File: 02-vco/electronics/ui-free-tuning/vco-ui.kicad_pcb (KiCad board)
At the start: 2 copper layers, 58 x 110 mm, 40 parts, among them J1 Conn_01x04, J2 Conn_02x05_Odd_Even, J3 Conn_02x03_Odd_Even, J4 Conn_01x02, J5 Conn_02x02_Counter_Clockwise, J6 Conn_01x06, U1 0203

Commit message: Added VCO output to default connector
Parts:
- J6: value Conn_01x06 -> Conn_01x07; footprint Connector_PinSocket_2.54mm:PinSocket_1x06_P2.54mm_Vertical -> Connector_PinSocket_2.54mm:PinSocket_1x07_P2.54mm_Vertical
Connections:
- J6 pad 6: OUT_DEFAULT -> OUT_OUT
- J_OUT1 pad T: Net-(J_OUT1-PadT) -> OUT_OUT
- U1 pad 1: Net-(J_OUT1-PadT) -> OUT_OUT
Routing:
- net OUT_OUT: track 0.00 -> 163.4 mm
- net Net-(J_OUT1-PadT): track 131.6 -> 0.00 mm
- net OUT_DEFAULT: track 39.9 -> 36.5 mm
- net SUB: track 36.9 -> 38.0 mm, vias 0 -> 2
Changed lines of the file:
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@@
 	(net 19 "EXTRA_DEFAULT")
 	(net 20 "OUT_DEFAULT")
-	(net 21 "Net-(J_OUT1-PadT)")
+	(net 21 "OUT_OUT")
 	(net 22 "Net-(J_PWM1-PadT)")
 	(net 23 "Net-(R1-Pad2)")
@@
 			(layers "*.Cu" "*.Mask")
 			(remove_unused_layers no)
-			(net 21 "Net-(J_OUT1-PadT)")
+			(net 21 "OUT_OUT")
 			(pinfunction "1")
 			(pintype "output")
@@
 			(layers "*.Cu" "*.Mask")
 			(remove_unused_layers no)
-			(net 21 "Net-(J_OUT1-PadT)")
+			(net 21 "OUT_OUT")
 			(pintype "bidirectional")
 		)
@@
 		)
 	)
-	(footprint "Connector_PinSocket_2.54mm:PinSocket_1x06_P2.54mm_Vertical"
+	(footprint "Connector_PinSocket_2.54mm:PinSocket_1x07_P2.54mm_Vertical"
 		(locked yes)
 		(layer "B.Cu")
 		(at 132.5 151 -90)
-		(descr "Through hole straight socket strip, 1x06, 2.54mm pitch, single row (from Kicad 4.0.7), script generated")
-		(tags "Through hole socket strip THT 1x06 2.54mm single row")
+		(descr "Through hole straight socket strip, 1x07, 2.54mm pitch, single row (from Kicad 4.0.7), script generated")
+		(tags "Through hole socket strip THT 1x07 2.54mm single row")
 		(property "Reference" "J6"
-			(at -1.966 -15.122 0)
-			(layer "B.SilkS")
+			(at 0 2.77 90)
+			(layer "User.1")
 			(effects
 				(font
@@
 			)
 		)
-		(property "Value" "Conn_01x06"
-			(at 0 -15.47 90)
+		(property "Value" "Conn_01x07"
+			(at 0 -18.01 90)
 			(layer "B.Fab")
 			(effects
@@
 			)
 		)
-		(property "Description" "Generic connector, single row, 01x06, script generated (kicad-library-utils/schlib/autogen/connector/)"
+		(property "Description" "Generic connector, single row, 01x07, script generated (kicad-library-utils/schlib/autogen/connector/)"
 			(at 0 0 90)
 			(layer "B.Fab")
@@
 		)
 		(property "Part URL" "https://mou.sr/4lnf48h"
-			(at 0 0 90)
+			(at 0 0 270)
 			(unlocked yes)
 			(layer "B.Fab")
@@
 		)
 		(property "Vendor" "Mouser"
-			(at 0 0 90)
+			(at 0 0 270)
 			(unlocked yes)
 			(layer "B.Fab")
@@
 		)
 		(property "LCSC" ""
-			(at 0 0 90)
+			(at 0 0 270)
 			(unlocked yes)
 			(layer "B.Fab")
@@
 			)
 		)
+		(property "Part No." ""
+			(at 0 0 270)
+			(unlocked yes)
+			(layer "B.Fab")
+			(hide yes)
+			(effects
+				(font
+					(size 1 1)
+					(thickness 0.15)
+				)
+				(justify mirror)
+			)
+		)
 		(property ki_fp_filters "Connector*:*_1x??_*")
 		(sheetname "/")
@@
 		(fp_line
 			(start -1.33 -1.27)
-			(end -1.33 -14.03)
+			(end -1.33 -16.57)
 			(stroke
 				(width 0.12)
@@
 		(fp_line
 			(start 1.33 -1.27)
-			(end 1.33 -14.03)
+			(end 1.33 -16.57)
 			(stroke
 				(width 0.12)
@@
 		)
 		(fp_line
-			(start -1.33 -14.03)
-			(end 1.33 -14.03)
+			(start -1.33 -16.57)
+			(end 1.33 -16.57)
 			(stroke
 				(width 0.12)
@@
 		(fp_line
 			(start 1.75 1.8)
-			(end 1.75 -14.45)
+			(end 1.75 -17)
 			(stroke
 				(width 0.05)
@@
 		)
 		(fp_line
-			(start -1.8 -14.45)
+			(start -1.8 -17)
 			(end -1.8 1.8)
 			(stroke
@@
 		)
 		(fp_line
-			(start 1.75 -14.45)
-			(end -1.8 -14.45)
+			(start 1.75 -17)
+			(end -1.8 -17)
 			(stroke
 				(width 0.05)
@@
 		(fp_line
 			(start 1.27 0.635)
-			(end 1.27 -13.97)
+			(end 1.27 -16.51)
 			(stroke
 				(width 0.1)
@@
 		)
 		(fp_line
-			(start -1.27 -13.97)
+			(start -1.27 -16.51)
 			(end -1.27 1.27)
 			(stroke
@@
 		)
 		(fp_line
-			(start 1.27 -13.97)
-			(end -1.27 -13.97)
+			(start 1.27 -16.51)
+			(end -1.27 -16.51)
 			(stroke
 				(width 0.1)
@@
 		)
 		(fp_text user "${REFERENCE}"
-			(at 0 -6.35 180)
+			(at 0 -7.62 0)
 			(layer "B.Fab")
 			(effects
@@
 			(layers "*.Cu" "*.Mask")
 			(remove_unused_layers no)
-			(net 20 "OUT_DEFAULT")
+			(net 21 "OUT_OUT")
 			(pinfunction "Pin_6")
 			(pintype "passive")
 		)
+		(pad "7" thru_hole circle
+			(at 0 -15.24 270)
+			(size 1.7 1.7)
+			(drill 1)
+			(layers "*.Cu" "*.Mask")
+			(remove_unused_layers no)
+			(net 20 "OUT_DEFAULT")
+			(pinfunction "Pin_7")
+			(pintype "passive")
+		)
 		(embedded_fonts no)
-		(model "${KICAD9_3DMODEL_DIR}/Connector_PinSocket_2.54mm.3dshapes/PinSocket_1x06_P2.54mm_Vertical.step"
+		(model "${KICAD9_3DMODEL_DIR}/Connector_PinSocket_2.54mm.3dshapes/PinSocket_1x07_P2.54mm_Vertical.step"
 			(offset
 				(xyz 0 0 0)
@@
 	(gr_rect
 		(start 131.112 149.664)
-		(end 146.606 152.331)
+		(end 149.019 152.331)
 		(stroke
 			(width 0.1)
@@
 	)
 	(gr_text "DEFAULTS"
-		(at 138.859 147.378 0)
+		(at 140.0655 147.378 0)
 		(layer "F.SilkS")
 		(effects
 			(font
-				(size 1 2.2)
+				(size 1 2.55)
 				(thickness 0.17)
 				(bold yes)
@@
 		)
 	)
+	(gr_text "OUT"
+		(at 148.003 149.029 0)
+		(layer "F.SilkS")
+		(effects
+			(font
+				(size 1 0.75)
+				(thickness 0.17)
+				(bold yes)
+			)
+			(justify bottom)
+		)
+	)
 	(gr_text "SUB"
 		(at 181.14 130.36 90)
@@
 	)
 	(segment
-		(start 161.465 151.188)
-		(end 160.322 152.331)
+		(start 161.592 131.63)
+		(end 161.592 142.933)
+		(width 0.508)
+		(layer "F.Cu")
+		(net 16)
+	)
+	(segment
+		(start 160.322 144.203)
+		(end 158.798 145.727)
+		(width 0.508)
+		(layer "F.Cu")
+		(net 16)
+	)
+	(segment
+		(start 153.591 148.902)
+		(end 153.591 149.918)
 		(width 0.508)
 		(layer "F.Cu")
@@
 	(segment
 		(start 164.64 128.582)
-		(end 161.465 131.757)
+		(end 161.592 131.63)
+		(width 0.508)
+		(layer "F.Cu")
+		(net 16)
+	)
+	(segment
+		(start 153.591 149.918)
+		(end 154.226 150.553)
 		(width 0.508)
 		(layer "F.Cu")
@@
 	)
 	(segment
-		(start 157.528 152.331)
-		(end 156.46 151.263)
+		(start 154.239 150.54)
+		(end 156.5 150.54)
 		(width 0.508)
 		(layer "F.Cu")
@@
 	)
 	(segment
-		(start 160.322 152.331)
-		(end 157.528 152.331)
+		(start 154.48 145.727)
+		(end 153.591 146.616)
 		(width 0.508)
 		(layer "F.Cu")
@@
 	)
 	(segment
-		(start 161.465 131.757)
-		(end 161.465 151.188)
+		(start 153.591 146.616)
+		(end 153.591 147.124)
 		(width 0.508)
 		(layer "F.Cu")
@@
 	)
 	(segment
-		(start 156.46 151.263)
-		(end 156.46 150.54)
+		(start 154.226 150.553)
+		(end 154.239 150.54)
 		(width 0.508)
 		(layer "F.Cu")
@@
 	)
 	(segment
+		(start 161.592 142.933)
+		(end 160.322 144.203)
+		(width 0.508)
+		(layer "F.Cu")
+		(net 16)
+	)
+	(segment
+		(start 158.798 145.727)
+		(end 154.48 145.727)
+		(width 0.508)
+		(layer "F.Cu")
+		(net 16)
+	)
+	(via
+		(at 153.591 148.902)
+		(size 0.8)
+		(drill 0.4)
+		(layers "F.Cu" "B.Cu")
+		(net 16)
+	)
+	(via
+		(at 153.591 147.124)
+		(size 0.8)
+		(drill 0.4)
+		(layers "F.Cu" "B.Cu")
+		(net 16)
+	)
+	(segment
+		(start 153.591 147.124)
+		(end 153.591 148.902)
+		(width 0.508)
+		(layer "B.Cu")
+		(net 16)
+	)
+	(segment
 		(start 163.878 126.042)
 		(end 170.99 126.042)
@@
 	)
 	(segment
-		(start 147.42 153.22)
-		(end 162.1 153.22)
+		(start 163.116 152.204)
+		(end 164.259 151.061)
 		(width 0.508)
 		(layer "F.Cu")
@@
 	)
 	(segment
-		(start 166.238 135.62)
-		(end 169 135.62)
+		(start 147.74 151)
+		(end 148.944 152.204)
 		(width 0.508)
 		(layer "F.Cu")
@@
 	)
 	(segment
-		(start 162.1 153.22)
-		(end 164.259 151.061)
+		(start 164.259 137.599)
+		(end 166.238 135.62)
 		(width 0.508)
 		(layer "F.Cu")
@@
 	)
 	(segment
-		(start 164.259 137.599)
-		(end 166.238 135.62)
+		(start 148.944 152.204)
+		(end 163.116 152.204)
 		(width 0.508)
 		(layer "F.Cu")
@@
 	)
 	(segment
-		(start 145.2 151)
-		(end 147.42 153.22)
+		(start 164.259 151.061)
+		(end 164.259 137.599)
 		(width 0.508)
 		(layer "F.Cu")
@@
 	)
 	(segment
-		(start 164.259 151.061)
-		(end 164.259 137.599)
+		(start 166.238 135.62)
+		(end 169 135.62)
 		(width 0.508)
 		(layer "F.Cu")
@@
 	)
 	(segment
+		(start 147.42 153.22)
+		(end 165.148 153.22)
+		(width 0.508)
+		(layer "F.Cu")
+		(net 21)
+	)
+	(segment
 		(start 144.32 60.002)
 		(end 144.322 60)
@@
 	)
 	(segment
+		(start 165.148 153.22)
+		(end 169 149.368)
+		(width 0.508)
+		(layer "F.Cu")
+		(net 21)
+	)
+	(segment
+		(start 145.2 151)
+		(end 147.42 153.22)
+		(width 0.508)
+		(layer "F.Cu")
+		(net 21)
+	)
+	(segment
 		(start 174.927 95.689)
 		(end 180.388 90.228)
 		(width 0.508)
 		(layer "F.Cu")
+		(net 21)
+	)
+	(segment
+		(start 169 149.368)
+		(end 169 143.92)
+		(width 0.508)
+		(layer "F.Cu")

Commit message: Updated VCO version number on PCB
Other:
- board text added: "HM-02 VCO UI V0.2 2025 OCT"
- board text removed: "HM-02 VCO UI V0.1 2025 JULY"
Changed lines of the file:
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@@
 		)
 	)
-	(gr_text "HM-02 VCO UI \nV0.1 2025 JULY"
+	(gr_text "HM-02 VCO UI \nV0.2 2025 OCT"
 		(at 153.394 68.5 0)
 		(layer "F.SilkS")
@@
 			(justify left bottom)
 		)
-		(render_cache "HM-02 VCO UI \nV0.1 2025 JULY" 0
+		(render_cache "HM-02 VCO UI \nV0.2 2025 OCT" 0
 			(polygon
 				(pts
@@
 			(polygon
 				(pts
-					(xy 156.903656 67.42633) (xy 156.903656 68.158161) (xy 156.61091 68.158161) (xy 156.61091 68.3045)
-					(xy 157.342741 68.3045) (xy 157.342741 68.158161) (xy 157.049994 68.158161) (xy 157.049994 67.133584)
-					(xy 156.903656 67.133584) (xy 156.903656 67.279992) (xy 156.61091 67.279992) (xy 156.61091 67.42633)
+					(xy 156.61091 68.011823) (xy 156.61091 68.3045) (xy 157.342741 68.3045) (xy 157.342741 68.158161)
+					(xy 156.757248 68.158161) (xy 156.757248 68.011823)
+				)
+			)
+			(polygon
+				(pts
+					(xy 157.196332 67.279992) (xy 157.196332 67.133584) (xy 156.757248 67.133584) (xy 156.757248 67.279992)
+				)
+			)
+			(polygon
+				(pts
+					(xy 157.196332 67.279992) (xy 157.196332 67.572739) (xy 157.342741 67.572739) (xy 157.342741 67.279992)
+				)
+			)
+			(polygon
+				(pts
+					(xy 156.757248 67.865415) (xy 156.757248 68.011823) (xy 156.903656 68.011823) (xy 156.903656 67.865415)
+				)
+			)
+			(polygon
+				(pts
+					(xy 156.61091 67.279992) (xy 156.61091 67.42633) (xy 156.757248 67.42633) (xy 156.757248 67.279992)
+				)
+			)
+			(polygon
+				(pts
+					(xy 157.049994 67.572739) (xy 157.049994 67.719077) (xy 157.196332 67.719077) (xy 157.196332 67.572739)
+				)
+			)
+			(polygon
+				(pts
+					(xy 156.903656 67.719077) (xy 156.903656 67.865415) (xy 157.049994 67.865415) (xy 157.049994 67.719077)
 				)
 			)
@@
 			(polygon
 				(pts
-					(xy 163.921916 68.158161) (xy 163.921916 68.011823) (xy 163.775578 68.011823) (xy 163.775578 68.158161)
+					(xy 163.775578 67.279992) (xy 163.775578 68.158161) (xy 163.921916 68.158161) (xy 163.921916 67.279992)
 				)
 			)
@@
 			(polygon
 				(pts
-					(xy 164.361001 67.279992) (xy 164.361001 68.158161) (xy 164.507409 68.158161) (xy 164.507409 67.133584)
-					(xy 164.068325 67.133584) (xy 164.068325 67.279992)
-				)
-			)
-			(polygon
-				(pts
-					(xy 164.799102 67.133584) (xy 164.799102 68.158161) (xy 164.945441 68.158161) (xy 164.945441 67.133584)
+					(xy 164.361001 67.279992) (xy 164.361001 68.158161) (xy 164.507409 68.158161) (xy 164.507409 67.279992)
+				)
+			)
+			(polygon
+				(pts
+					(xy 163.921916 67.133584) (xy 163.921916 67.279992) (xy 164.361001 67.279992) (xy 164.361001 67.133584)
+				)
+			)
+			(polygon
+				(pts
+					(xy 164.799102 67.279992) (xy 164.799102 68.158161) (xy 164.945441 68.158161) (xy 164.945441 67.279992)
 				)
 			)
@@
 			(polygon
 				(pts
-					(xy 165.384525 67.133584) (xy 165.384525 68.158161) (xy 165.530933 68.158161) (xy 165.530933 67.133584)
-				)
-			)
-			(polygon
-				(pts
-					(xy 165.822627 67.133584) (xy 165.822627 68.3045) (xy 166.554457 68.3045) (xy 166.554457 68.158161)
-					(xy 165.968965 68.158161) (xy 165.968965 67.133584)
-				)
-			)
-			(polygon
-				(pts
-					(xy 166.846151 67.133584) (xy 166.846151 67.572739) (xy 166.992489 67.572739) (xy 166.992489 67.133584)
-				)
-			)
-			(polygon
-				(pts
-					(xy 167.431573 67.133584) (xy 167.431573 67.572739) (xy 167.577982 67.572739) (xy 167.577982 67.133584)
-				)
-			)
-			(polygon
-				(pts
-					(xy 167.138897 67.719077) (xy 167.138897 68.3045) (xy 167.285235 68.3045) (xy 167.285235 67.719077)
-				)
-			)
-			(polygon
-				(pts
-					(xy 166.992489 67.572739) (xy 166.992489 67.719077) (xy 167.138897 67.719077) (xy 167.138897 67.572739)
-				)
-			)
-			(polygon
-				(pts
-					(xy 167.285235 67.572739) (xy 167.285235 67.719077) (xy 167.431573 67.719077) (xy 167.431573 67.572739)
-				)
-			)
+					(xy 165.384525 68.011823) (xy 165.384525 68.158161) (xy 165.530933 68.158161) (xy 165.530933 68.011823)
+				)
+			)
+			(polygon
+				(pts
+					(xy 164.945441 67.133584) (xy 164.945441 67.279992) (xy 165.384525 67.279992) (xy 165.384525 67.133584)
+				)
+			)
+			(polygon
+				(pts
+					(xy 165.384525 67.279992) (xy 165.384525 67.42633) (xy 165.530933 67.42633) (xy 165.530933 67.279992)
+				)
+			)
+			(polygon
+				(pts
+					(xy 165.822627 67.133584) (xy 165.822627 67.279992) (xy 166.115373 67.279992) (xy 166.115373 68.3045)
+					(xy 166.261711 68.3045) (xy 166.261711 67.279992) (xy 166.554457 67.279992) (xy 166.554457 67.133584)
+				)
+			)

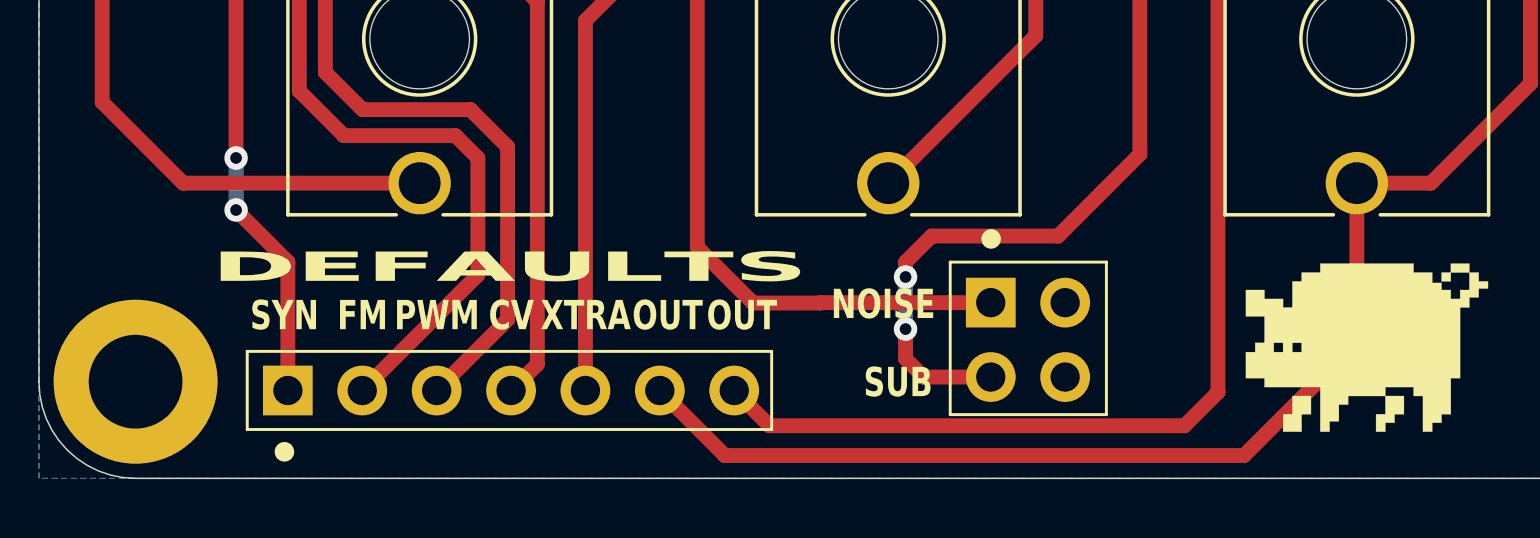
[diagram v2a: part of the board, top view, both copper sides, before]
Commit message: Added CV output to VCO default patch
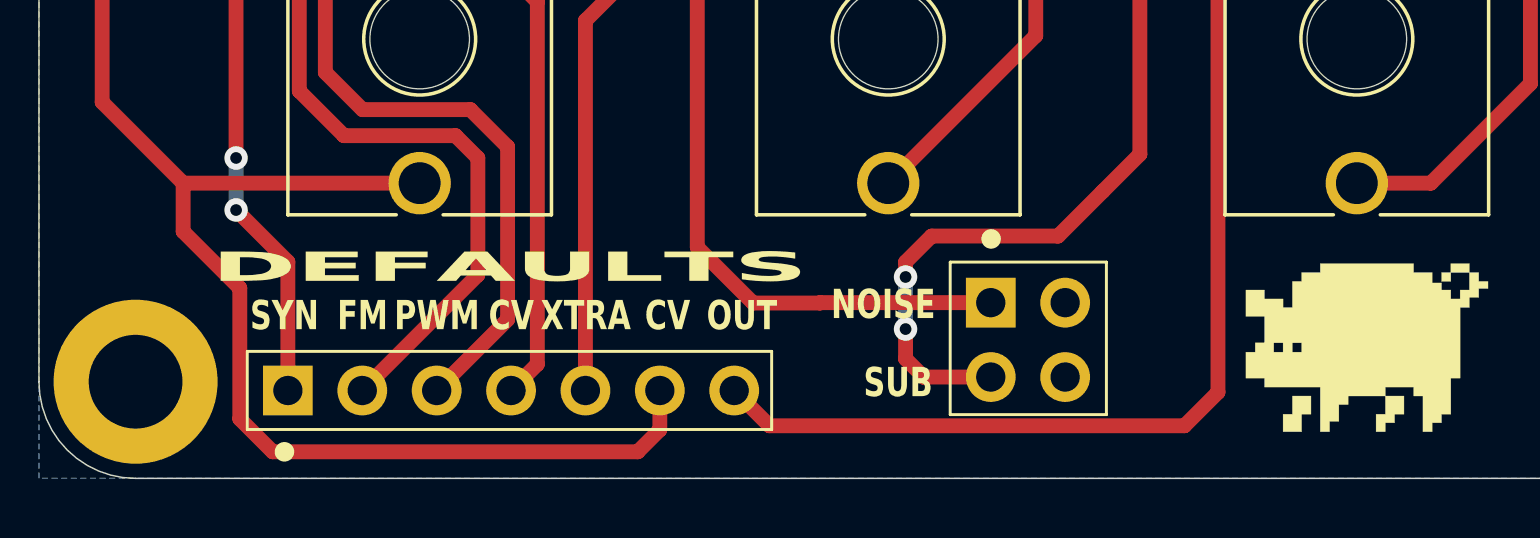
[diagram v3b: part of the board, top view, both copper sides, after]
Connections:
- J6 pad 6: OUT_OUT -> CV_INPUT
- J_CV1 pad T: Net-(J_CV1-PadT) -> CV_INPUT
- J_OUT1 pad T: OUT_OUT -> Net-(J_OUT1-PadT)
- R3 pad 1: Net-(J_CV1-PadT) -> CV_INPUT
- U1 pad 1: OUT_OUT -> Net-(J_OUT1-PadT)
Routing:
- net OUT_OUT: track 163.4 -> 0.00 mm
- net Net-(J_OUT1-PadT): track 0.00 -> 131.6 mm
- net CV_INPUT: track 0.00 -> 103.8 mm
- net Net-(J_CV1-PadT): track 78.5 -> 0.00 mm
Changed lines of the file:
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@@
 	(net 16 "SUB")
 	(net 17 "Net-(JP1-C)")
-	(net 18 "Net-(J_CV1-PadT)")
+	(net 18 "CV_INPUT")
 	(net 19 "EXTRA_DEFAULT")
 	(net 20 "OUT_DEFAULT")
-	(net 21 "OUT_OUT")
+	(net 21 "Net-(J_OUT1-PadT)")
 	(net 22 "Net-(J_PWM1-PadT)")
 	(net 23 "Net-(R1-Pad2)")
@@
 			(layers "*.Cu" "*.Mask")
 			(remove_unused_layers no)
-			(net 21 "OUT_OUT")
+			(net 21 "Net-(J_OUT1-PadT)")
 			(pinfunction "1")
 			(pintype "output")
@@
 			(layers "*.Cu" "*.Mask")
 			(remove_unused_layers no)
-			(net 18 "Net-(J_CV1-PadT)")
+			(net 18 "CV_INPUT")
 			(pintype "bidirectional")
 		)
@@
 			(layers "*.Cu" "*.Mask")
 			(remove_unused_layers no)
-			(net 21 "OUT_OUT")
+			(net 21 "Net-(J_OUT1-PadT)")
 			(pintype "bidirectional")
 		)
@@
 			(layers "*.Cu" "*.Mask")
 			(remove_unused_layers no)
-			(net 18 "Net-(J_CV1-PadT)")
+			(net 18 "CV_INPUT")
 			(pintype "passive")
 		)
@@
 			(layers "*.Cu" "*.Mask")
 			(remove_unused_layers no)
-			(net 21 "OUT_OUT")
+			(net 18 "CV_INPUT")
 			(pinfunction "Pin_6")
 			(pintype "passive")
@@
 		)
 	)
-	(gr_text "OUT"
+	(gr_text "CV"
 		(at 145.463 149.029 0)
 		(layer "F.SilkS" knockout)
@@
 	)
 	(segment
+		(start 130.858 147.505)
+		(end 128.924 145.571)
+		(width 0.508)
+		(layer "F.Cu")
+		(net 18)
+	)
+	(segment
+		(start 130.858 151.968)
+		(end 130.858 147.505)
+		(width 0.508)
+		(layer "F.Cu")
+		(net 18)
+	)
+	(segment
+		(start 144.447 153.093)
+		(end 131.983 153.093)
+		(width 0.508)
+		(layer "F.Cu")
+		(net 18)
+	)
+	(segment
+		(start 131.983 153.093)
+		(end 130.858 151.968)
+		(width 0.508)
+		(layer "F.Cu")
+		(net 18)
+	)
+	(segment
 		(start 126.159 79.306)
 		(end 126.159 141.155)
@@
 	)
 	(segment
+		(start 145.2 152.34)
+		(end 144.447 153.093)
+		(width 0.508)
+		(layer "F.Cu")
+		(net 18)
+	)
+	(segment
 		(start 128.924 143.92)
 		(end 137 143.92)
@@
 	)
 	(segment
+		(start 145.2 151)
+		(end 145.2 152.34)
+		(width 0.508)
+		(layer "F.Cu")
+		(net 18)
+	)
+	(segment
+		(start 128.924 145.571)
+		(end 128.924 143.92)
+		(width 0.508)
+		(layer "F.Cu")
+		(net 18)
+	)
+	(segment
 		(start 142.66 138.37)
 		(end 142.66 151)
@@
 	)
 	(segment
-		(start 163.116 152.204)
-		(end 164.259 151.061)
+		(start 147.74 151)
+		(end 148.944 152.204)
 		(width 0.508)
 		(layer "F.Cu")
@@
 	)
 	(segment
-		(start 147.74 151)
-		(end 148.944 152.204)
+		(start 166.238 135.62)
+		(end 169 135.62)
 		(width 0.508)
 		(layer "F.Cu")
@@
 	)
 	(segment
-		(start 148.944 152.204)
-		(end 163.116 152.204)
+		(start 164.259 151.061)
+		(end 164.259 137.599)
 		(width 0.508)
 		(layer "F.Cu")
@@
 	)
 	(segment
-		(start 164.259 151.061)
-		(end 164.259 137.599)
+		(start 148.944 152.204)
+		(end 163.116 152.204)
 		(width 0.508)
 		(layer "F.Cu")
@@
 	)
 	(segment
-		(start 166.238 135.62)
-		(end 169 135.62)
+		(start 163.116 152.204)
+		(end 164.259 151.061)
 		(width 0.508)
 		(layer "F.Cu")
@@
 	)
 	(segment
-		(start 147.42 153.22)
-		(end 165.148 153.22)
-		(width 0.508)
-		(layer "F.Cu")
-		(net 21)
-	)
-	(segment
 		(start 144.32 60.002)
 		(end 144.322 60)
@@
 	)
 	(segment
-		(start 165.148 153.22)
-		(end 169 149.368)
-		(width 0.508)
-		(layer "F.Cu")
-		(net 21)
-	)
-	(segment
-		(start 145.2 151)
-		(end 147.42 153.22)
-		(width 0.508)
-		(layer "F.Cu")
-		(net 21)
-	)
-	(segment
 		(start 174.927 95.689)
 		(end 180.388 90.228)
 		(width 0.508)
 		(layer "F.Cu")
-		(net 21)
-	)
-	(segment
-		(start 169 149.368)
-		(end 169 143.92)
-		(width 0.508)
-		(layer "F.Cu")
